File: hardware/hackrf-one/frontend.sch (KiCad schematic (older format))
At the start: 132 parts, among them J2 RF-SHIELD-FRAME, J3 RF-SHIELD-COVER, P13 GPO1, P17 GPO6, P19 GPO3, P21 REF_IN, P27 MIXER_SDATA, P31 MIXER_SCLK, P32 MIXER_ENX, P33 MIXER_RESETX, P34 MIX_BYPASS, P35 !MIX_BYPASS, P4 ANTENNA, P42 TX, P43 RX, P44 HP, P45 LP, P46 TX_MIX_BP, P47 RX_MIX_BP, P48 TX_AMP, P49 RX_AMP, P50 AMP_BYPASS, P51 !TX_AMP_PWR, P52 !RX_AMP_PWR, P6 GPO4, P7 GPO2, Q1 MOSFET_P, Q2 MOSFET_P, T1 MIX_IN_BALUN, T2 MIX_OUT_BALUN, U1 SKY13350, U10 SKY13350, U11 SKY13350, U12 SKY13317, U13 MGA-81563, U14 SKY13317, U2 SKY13350, U25 MGA-81563, U3 RX_LOWPASS_FILTER, U4 RFFC5072, U5 SKY13350, U6 SKY13350, U7 SKY13350, U8 RX_HIGHPASS_FILTER, U9 SKY13317

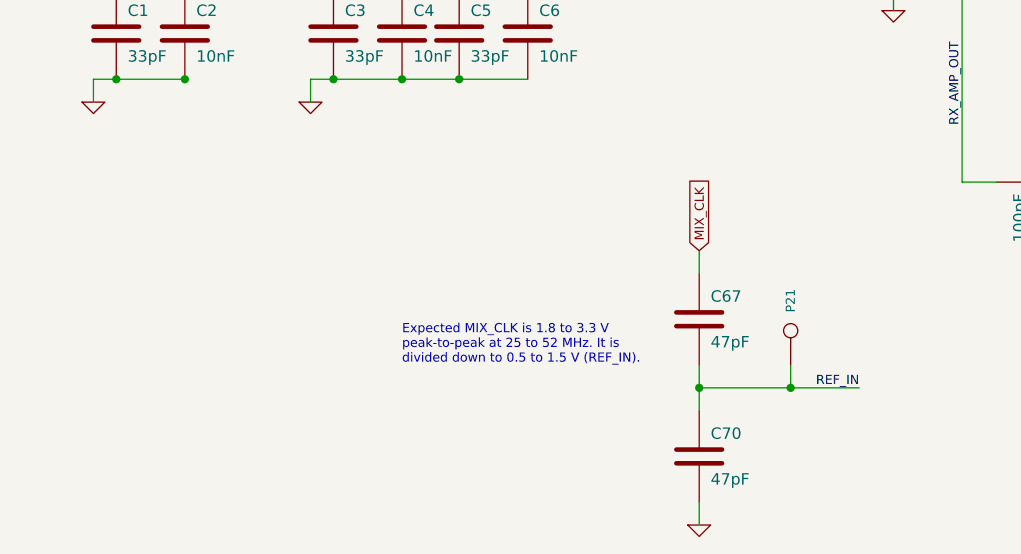
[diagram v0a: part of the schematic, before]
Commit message: more decoupling caps
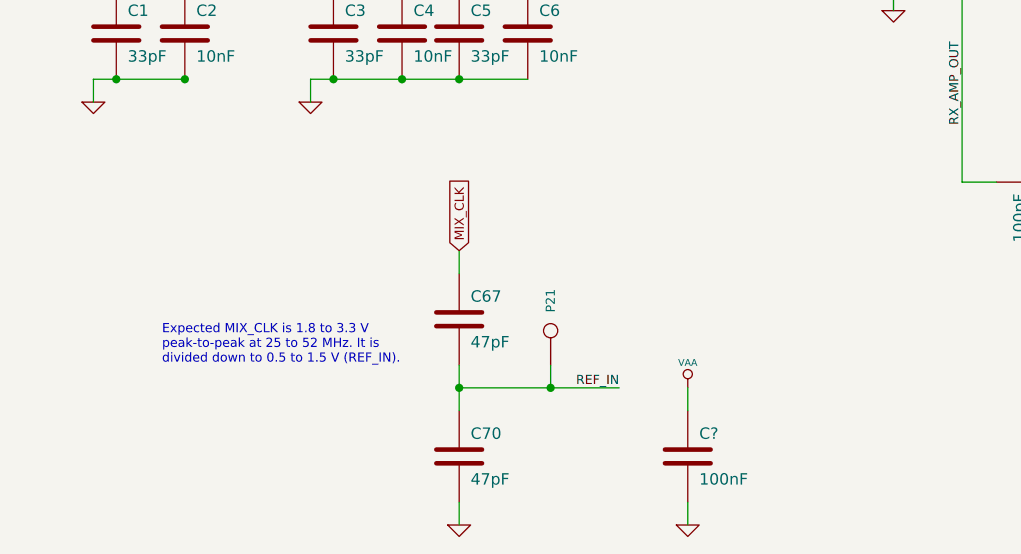
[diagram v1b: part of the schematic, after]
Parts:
- added C?: 100nF, symbol C
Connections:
- net GND: now also C?.2
- net VAA: now also C?.1
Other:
- moved on the sheet: C67, C70, P21
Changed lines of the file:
@@
 Wire Wire Line
 	15700 9150 15700 9050
-Connection ~ 7350 9700
+Connection ~ 6300 9700
 Wire Wire Line
-	8050 9700 7350 9700
+	7000 9700 6300 9700
 Wire Wire Line
-	7350 9600 7350 9800
+	6300 9600 6300 9800
 Wire Wire Line
 	7100 3750 7100 3850
@@
 Connection ~ 7100 4650
 Wire Wire Line
-	7350 10300 7350 10200
+	6300 10300 6300 10200
 Wire Wire Line
-	7350 9200 7350 9100
+	6300 9200 6300 9100
 Wire Wire Line
 	4100 5650 4100 5550
@@
 Text GLabel 7200 4450 2    40   Input ~ 0
 MIXER_SDATA
-Text GLabel 7350 9100 1    40   Input ~ 0
+Text GLabel 6300 9100 1    40   Input ~ 0
 MIX_CLK
 $Comp
@@
 	1    0    0    -1
 $EndComp
-Text Notes 6050 9600 0    40   ~ 0
+Text Notes 5000 9600 0    40   ~ 0
 Expected MIX_CLK is 1.8 to 3.3 V\npeak-to-peak at 25 to 52 MHz. It is\ndivided down to 0.5 to 1.5 V (REF_IN).
 $Comp
 L C C70
 U 1 1 4FB3CC76
-P 7350 10000
-F 0 "C70" H 7400 10100 50  0000 L CNN
-F 1 "47pF" H 7400 9900 50  0000 L CNN
-F 2 "" H 7350 10000 60  0001 C CNN
-F 3 "" H 7350 10000 60  0001 C CNN
-F 4 "Murata" H 7350 9400 60  0001 C CNN "Manufacturer"
-F 5 "GRM1555C1H470JZ01D" H 7350 9400 60  0001 C CNN "Part Number"
-F 6 "CAP CER 47PF 50V 5% NP0 0402" H 7350 9400 60  0001 C CNN "Description"
-	1    7350 10000
+P 6300 10000
+F 0 "C70" H 6350 10100 50  0000 L CNN
+F 1 "47pF" H 6350 9900 50  0000 L CNN
+F 2 "" H 6300 10000 60  0001 C CNN
+F 3 "" H 6300 10000 60  0001 C CNN
+F 4 "Murata" H 6300 9400 60  0001 C CNN "Manufacturer"
+F 5 "GRM1555C1H470JZ01D" H 6300 9400 60  0001 C CNN "Part Number"
+F 6 "CAP CER 47PF 50V 5% NP0 0402" H 6300 9400 60  0001 C CNN "Description"
+	1    6300 10000
 	1    0    0    -1
 $EndComp
@@
 	1    0    0    -1
 $EndComp
-Text Label 8050 9700 2    40   ~ 0
+Text Label 7000 9700 2    40   ~ 0
 REF_IN
 $Comp
 L GND #PWR058
 U 1 1 4FB3CC7B
-P 7350 10300
-F 0 "#PWR058" H 7350 10300 30  0001 C CNN
-F 1 "GND" H 7350 10230 30  0001 C CNN
-F 2 "" H 7350 10300 60  0001 C CNN
-F 3 "" H 7350 10300 60  0001 C CNN
-	1    7350 10300
+P 6300 10300
+F 0 "#PWR058" H 6300 10300 30  0001 C CNN
+F 1 "GND" H 6300 10230 30  0001 C CNN
+F 2 "" H 6300 10300 60  0001 C CNN
+F 3 "" H 6300 10300 60  0001 C CNN
+	1    6300 10300
 	1    0    0    -1
 $EndComp
@@
 L C C67
 U 1 1 4FAECD45
-P 7350 9400
-F 0 "C67" H 7400 9500 50  0000 L CNN
-F 1 "47pF" H 7400 9300 50  0000 L CNN
-F 2 "" H 7350 9400 60  0001 C CNN
-F 3 "" H 7350 9400 60  0001 C CNN
-F 4 "Murata" H 7350 9400 60  0001 C CNN "Manufacturer"
-F 5 "GRM1555C1H470JZ01D" H 7350 9400 60  0001 C CNN "Part Number"
-F 6 "CAP CER 47PF 50V 5% NP0 0402" H 7350 9400 60  0001 C CNN "Description"
-	1    7350 9400
+P 6300 9400
+F 0 "C67" H 6350 9500 50  0000 L CNN
+F 1 "47pF" H 6350 9300 50  0000 L CNN
+F 2 "" H 6300 9400 60  0001 C CNN
+F 3 "" H 6300 9400 60  0001 C CNN
+F 4 "Murata" H 6300 9400 60  0001 C CNN "Manufacturer"
+F 5 "GRM1555C1H470JZ01D" H 6300 9400 60  0001 C CNN "Part Number"
+F 6 "CAP CER 47PF 50V 5% NP0 0402" H 6300 9400 60  0001 C CNN "Description"
+	1    6300 9400
 	1    0    0    -1
 $EndComp
@@
 L CONN_1 P21
 U 1 1 528044E0
-P 7750 9450
-F 0 "P21" H 7830 9450 40  0000 L CNN
-F 1 "REF_IN" H 7750 9505 30  0001 C CNN
-F 2 "" H 7750 9450 60  0001 C CNN
-F 3 "" H 7750 9450 60  0001 C CNN
-F 4 "DNP" H 7750 9450 60  0001 C CNN "Note"
-	1    7750 9450
+P 6700 9450
+F 0 "P21" H 6780 9450 40  0000 L CNN
+F 1 "REF_IN" H 6700 9505 30  0001 C CNN
+F 2 "" H 6700 9450 60  0001 C CNN
+F 3 "" H 6700 9450 60  0001 C CNN
+F 4 "DNP" H 6700 9450 60  0001 C CNN "Note"
+	1    6700 9450
 	0    -1   -1   0
 $EndComp
@@
 	3600 10200 3700 10200
 Wire Wire Line
-	7750 9600 7750 9700
-Connection ~ 7750 9700
+	6700 9600 6700 9700
+Connection ~ 6700 9700
+$Comp
+L C C?
+U 1 1 5281BF94
+P 7300 10000
+F 0 "C?" H 7350 10100 50  0000 L CNN
+F 1 "100nF" H 7350 9900 50  0000 L CNN
+F 2 "" H 7300 10000 60  0001 C CNN
+F 3 "" H 7300 10000 60  0001 C CNN
+F 4 "Murata" H 7300 10000 60  0001 C CNN "Manufacturer"
+F 5 "GRM155R61A104KA01D" H 7300 10000 60  0001 C CNN "Part Number"
+F 6 "CAP CER 0.1UF 10V 10% X5R 0402" H 7300 10000 60  0001 C CNN "Description"
+	1    7300 10000
+	1    0    0    -1
+$EndComp
+$Comp
+L GND #PWR?
+U 1 1 5281BF9C
+P 7300 10300
+F 0 "#PWR?" H 7300 10300 30  0001 C CNN
+F 1 "GND" H 7300 10230 30  0001 C CNN
+F 2 "" H 7300 10300 60  0000 C CNN
+F 3 "" H 7300 10300 60  0000 C CNN
+	1    7300 10300
+	1    0    0    -1
+$EndComp
+$Comp
+L VAA #PWR?
+U 1 1 5281BFB9
+P 7300 9700
+F 0 "#PWR?" H 7300 9760 30  0001 C CNN
+F 1 "VAA" H 7300 9810 30  0000 C CNN
+F 2 "" H 7300 9700 60  0001 C CNN
+F 3 "" H 7300 9700 60  0001 C CNN
+	1    7300 9700
+	1    0    0    -1
+$EndComp
+Wire Wire Line
+	7300 9700 7300 9800
+Wire Wire Line
+	7300 10200 7300 10300
 $EndSCHEMATC

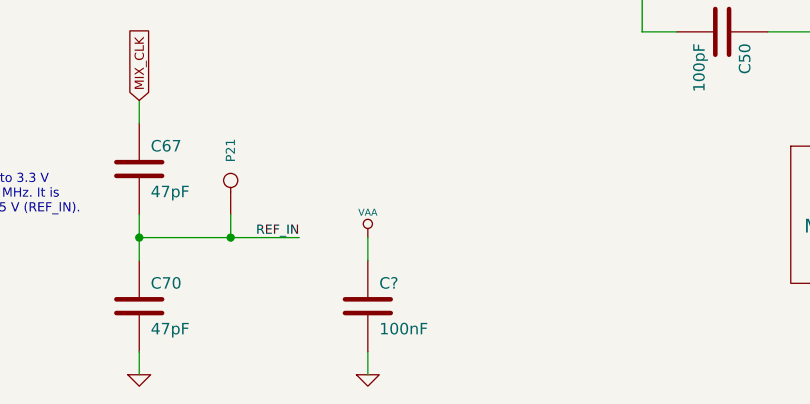
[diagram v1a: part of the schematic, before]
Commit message: GND test points
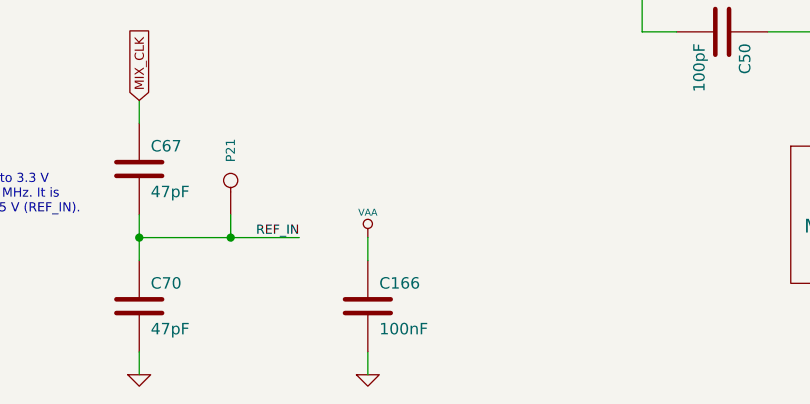
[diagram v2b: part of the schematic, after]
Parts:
- gave numbers to parts that had none: 1
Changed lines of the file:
@@
 Connection ~ 6700 9700
 $Comp
-L C C?
+L C C166
 U 1 1 5281BF94
 P 7300 10000
-F 0 "C?" H 7350 10100 50  0000 L CNN
+F 0 "C166" H 7350 10100 50  0000 L CNN
 F 1 "100nF" H 7350 9900 50  0000 L CNN
 F 2 "" H 7300 10000 60  0001 C CNN
@@
 $EndComp
 $Comp
-L GND #PWR?
+L GND #PWR081
 U 1 1 5281BF9C
 P 7300 10300
-F 0 "#PWR?" H 7300 10300 30  0001 C CNN
+F 0 "#PWR081" H 7300 10300 30  0001 C CNN
 F 1 "GND" H 7300 10230 30  0001 C CNN
 F 2 "" H 7300 10300 60  0000 C CNN
@@
 $EndComp
 $Comp
-L VAA #PWR?
+L VAA #PWR082
 U 1 1 5281BFB9
 P 7300 9700
-F 0 "#PWR?" H 7300 9760 30  0001 C CNN
+F 0 "#PWR082" H 7300 9760 30  0001 C CNN
 F 1 "VAA" H 7300 9810 30  0000 C CNN
 F 2 "" H 7300 9700 60  0001 C CNN

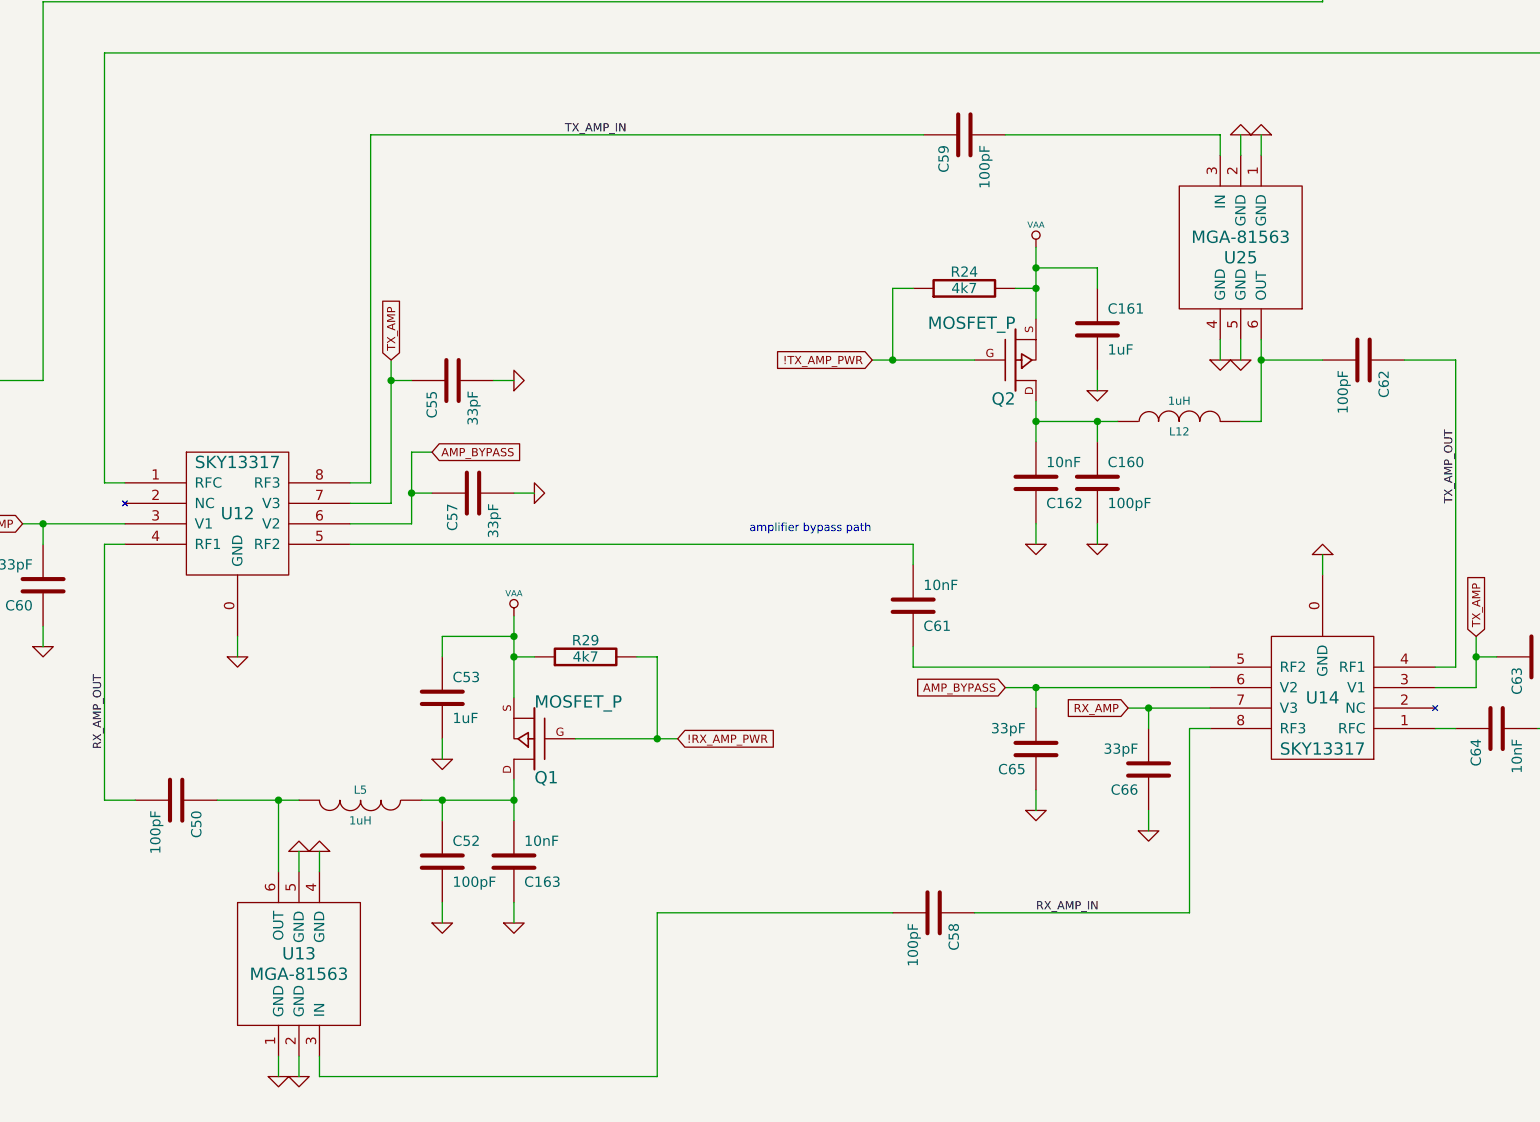
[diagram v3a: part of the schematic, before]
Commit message: changed some capacitor values to improve low frequency performance
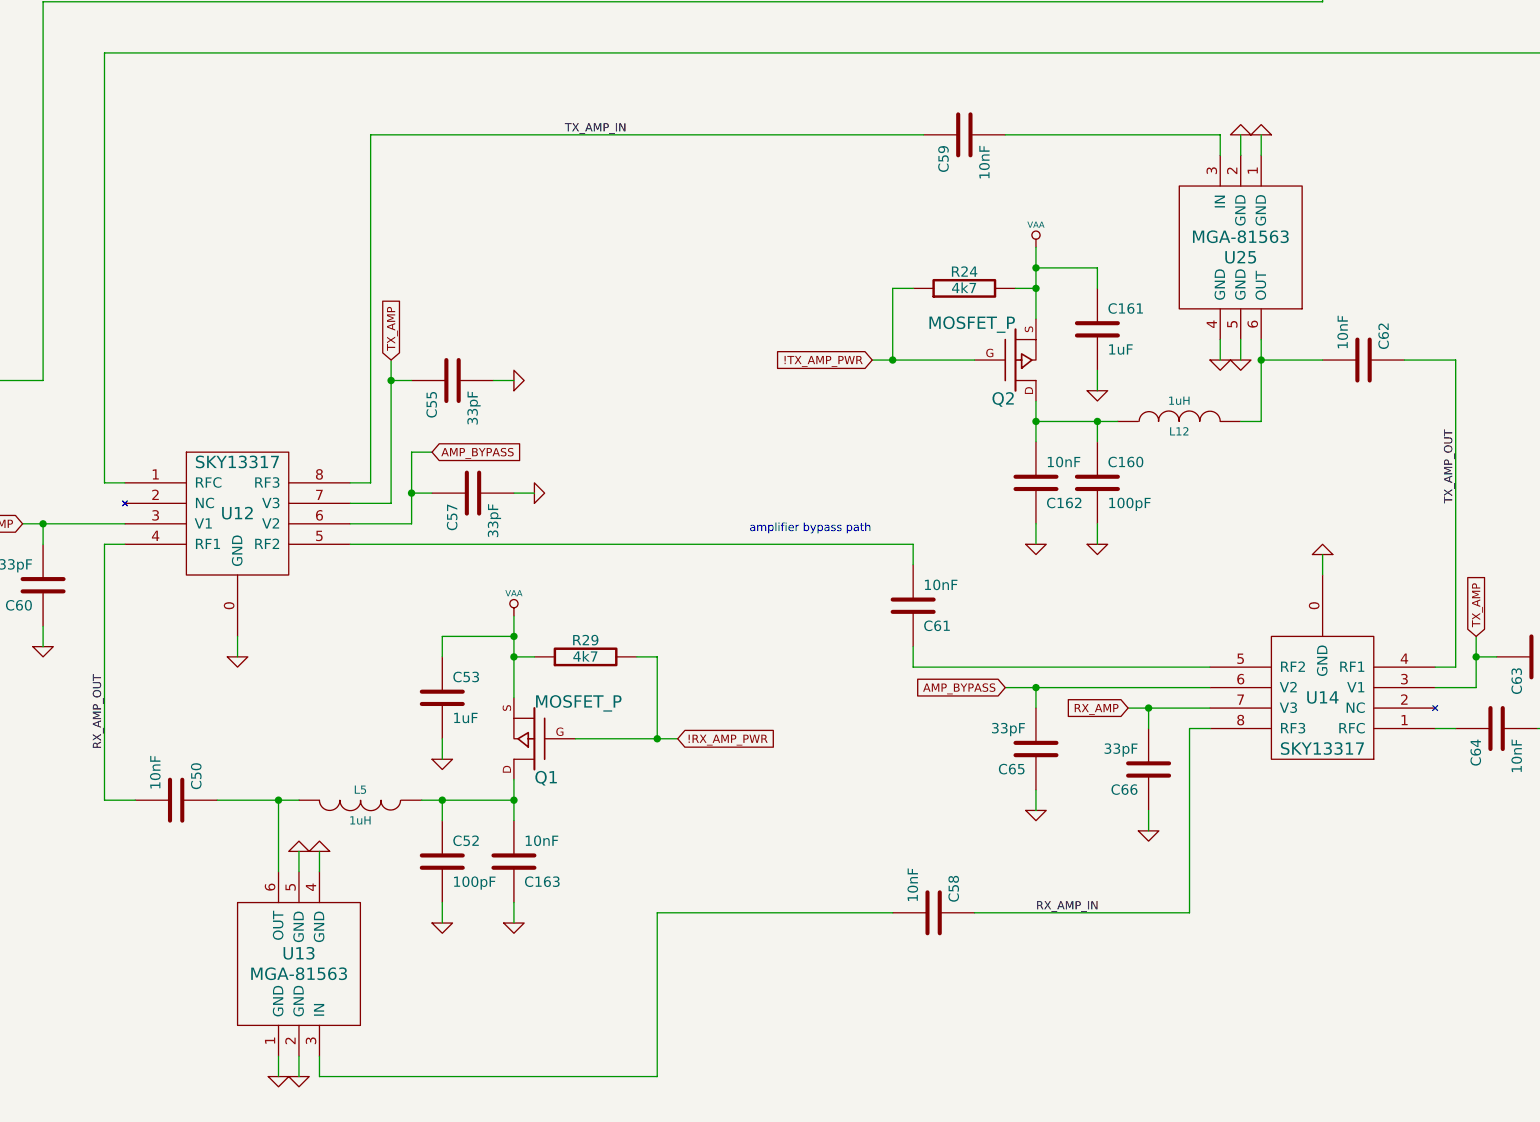
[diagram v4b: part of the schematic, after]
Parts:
- C50, C58, C59, C62: value 100pF -> 10nF; Description CAP CER 100PF 50V 5% NP0 0402 -> CAP CER 10000PF 16V 10% X7R 0402; Part Number GRM1555C1H101JZ01D -> GRM155R71C103KA01D
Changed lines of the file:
@@
 Sheet 2 4
 Title "HackRF One frontend"
-Date "17 nov 2013"
+Date "21 nov 2013"
 Rev ""
 Comp "Copyright 2012 Michael Ossmann"
@@
 RX_AMP_IN
 $Comp
-L C C62
-U 1 1 502E6667
-P 14650 6650
-F 0 "C62" H 14700 6750 50  0000 L CNN
-F 1 "100pF" H 14700 6550 50  0000 L CNN
-F 2 "" H 14650 6650 60  0001 C CNN
-F 3 "" H 14650 6650 60  0001 C CNN
-F 4 "Murata" H 17650 8200 60  0001 C CNN "Manufacturer"
-F 5 "GRM1555C1H101JZ01D" H 17650 8200 60  0001 C CNN "Part Number"
-F 6 "CAP CER 100PF 50V 5% NP0 0402" H 17650 8200 60  0001 C CNN "Description"
-	1    14650 6650
-	0    1    1    0
-$EndComp
-$Comp
-L C C59
-U 1 1 502E665E
-P 12700 5550
-F 0 "C59" H 12750 5650 50  0000 L CNN
-F 1 "100pF" H 12750 5450 50  0000 L CNN
-F 2 "" H 12700 5550 60  0001 C CNN
-F 3 "" H 12700 5550 60  0001 C CNN
-F 4 "Murata" H 15700 7100 60  0001 C CNN "Manufacturer"
-F 5 "GRM1555C1H101JZ01D" H 15700 7100 60  0001 C CNN "Part Number"
-F 6 "CAP CER 100PF 50V 5% NP0 0402" H 15700 7100 60  0001 C CNN "Description"
-	1    12700 5550
-	0    -1   1    0
-$EndComp
-$Comp
 L GND #PWR036
 U 1 1 502E6209
@@
 $EndComp
 $Comp
-L C C50
-U 1 1 502E5F58
-P 8850 8800
-F 0 "C50" H 8900 8900 50  0000 L CNN
-F 1 "100pF" H 8900 8700 50  0000 L CNN
-F 2 "" H 8850 8800 60  0001 C CNN
-F 3 "" H 8850 8800 60  0001 C CNN
-F 4 "Murata" H 11850 10350 60  0001 C CNN "Manufacturer"
-F 5 "GRM1555C1H101JZ01D" H 11850 10350 60  0001 C CNN "Part Number"
-F 6 "CAP CER 100PF 50V 5% NP0 0402" H 11850 10350 60  0001 C CNN "Description"
-	1    8850 8800
-	0    1    1    0
-$EndComp
-$Comp
-L C C58
-U 1 1 502E5F55
-P 12550 9350
-F 0 "C58" H 12600 9450 50  0000 L CNN
-F 1 "100pF" H 12600 9250 50  0000 L CNN
-F 2 "" H 12550 9350 60  0001 C CNN
-F 3 "" H 12550 9350 60  0001 C CNN
-F 4 "Murata" H 15550 10900 60  0001 C CNN "Manufacturer"
-F 5 "GRM1555C1H101JZ01D" H 15550 10900 60  0001 C CNN "Part Number"
-F 6 "CAP CER 100PF 50V 5% NP0 0402" H 15550 10900 60  0001 C CNN "Description"
-	1    12550 9350
-	0    1    1    0
-$EndComp
-$Comp
 L MGA-81563 U13
 U 1 1 502DE480
@@
 Wire Wire Line
 	7300 10200 7300 10300
+$Comp
+L C C58
+U 1 1 528EA8DE
+P 12550 9350
+F 0 "C58" H 12600 9450 50  0000 L CNN
+F 1 "10nF" H 12600 9250 50  0000 L CNN
+F 2 "" H 12550 9350 60  0001 C CNN
+F 3 "" H 12550 9350 60  0001 C CNN
+F 4 "Murata" H 18950 8100 60  0001 C CNN "Manufacturer"
+F 5 "GRM155R71C103KA01D" H 18950 8100 60  0001 C CNN "Part Number"
+F 6 "CAP CER 10000PF 16V 10% X7R 0402" H 18950 8100 60  0001 C CNN "Description"
+	1    12550 9350
+	0    1    -1   0
+$EndComp
+$Comp
+L C C50
+U 1 1 528EA90E
+P 8850 8800
+F 0 "C50" H 8900 8900 50  0000 L CNN
+F 1 "10nF" H 8900 8700 50  0000 L CNN
+F 2 "" H 8850 8800 60  0001 C CNN
+F 3 "" H 8850 8800 60  0001 C CNN
+F 4 "Murata" H 15250 7550 60  0001 C CNN "Manufacturer"
+F 5 "GRM155R71C103KA01D" H 15250 7550 60  0001 C CNN "Part Number"
+F 6 "CAP CER 10000PF 16V 10% X7R 0402" H 15250 7550 60  0001 C CNN "Description"
+	1    8850 8800
+	0    1    -1   0
+$EndComp
+$Comp
+L C C59
+U 1 1 528EA93E
+P 12700 5550
+F 0 "C59" H 12750 5650 50  0000 L CNN
+F 1 "10nF" H 12750 5450 50  0000 L CNN
+F 2 "" H 12700 5550 60  0001 C CNN
+F 3 "" H 12700 5550 60  0001 C CNN
+F 4 "Murata" H 19100 4300 60  0001 C CNN "Manufacturer"
+F 5 "GRM155R71C103KA01D" H 19100 4300 60  0001 C CNN "Part Number"
+F 6 "CAP CER 10000PF 16V 10% X7R 0402" H 19100 4300 60  0001 C CNN "Description"
+	1    12700 5550
+	0    -1   1    0
+$EndComp
+$Comp
+L C C62
+U 1 1 528EA96E
+P 14650 6650
+F 0 "C62" H 14700 6750 50  0000 L CNN
+F 1 "10nF" H 14700 6550 50  0000 L CNN
+F 2 "" H 14650 6650 60  0001 C CNN
+F 3 "" H 14650 6650 60  0001 C CNN
+F 4 "Murata" H 21050 5400 60  0001 C CNN "Manufacturer"
+F 5 "GRM155R71C103KA01D" H 21050 5400 60  0001 C CNN "Part Number"
+F 6 "CAP CER 10000PF 16V 10% X7R 0402" H 21050 5400 60  0001 C CNN "Description"
+	1    14650 6650
+	0    1    -1   0
+$EndComp
 $EndSCHEMATC
